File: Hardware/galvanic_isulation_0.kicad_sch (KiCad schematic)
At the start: 14 parts

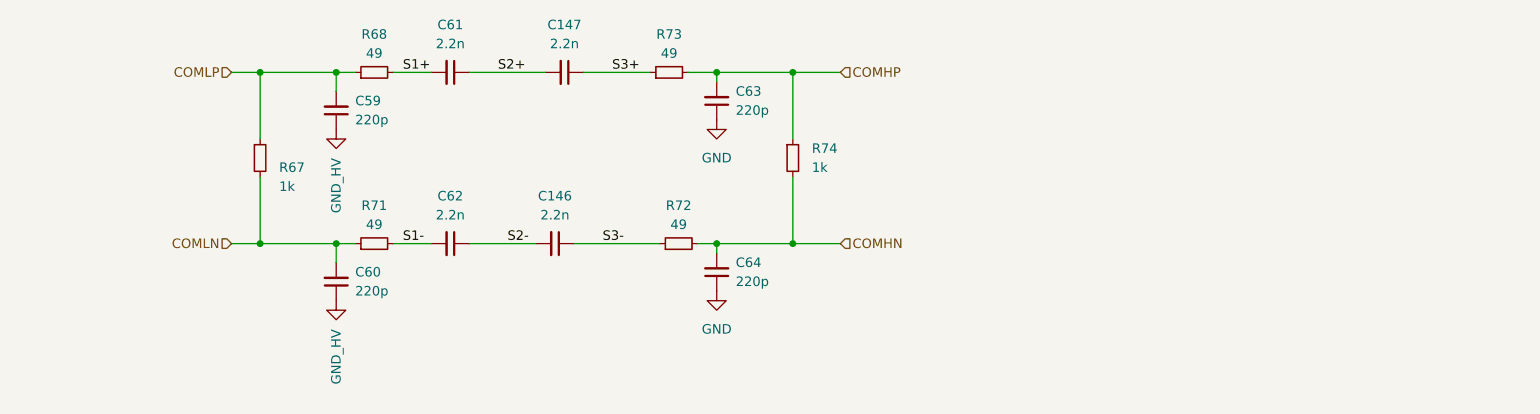
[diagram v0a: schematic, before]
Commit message: Bms plug and play, 2nd iteration with the same pinout
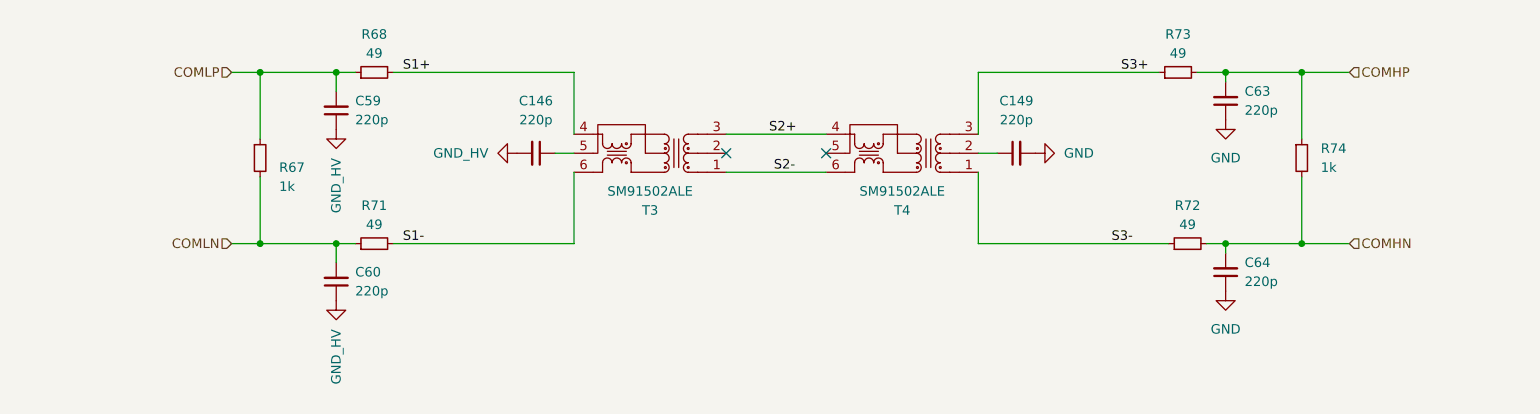
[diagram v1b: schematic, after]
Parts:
- removed C147, C61, C62: 2.2n, footrpint:CAPC5728X280N, symbol Device:C_Small
- added C149: 220p, Capacitor_SMD:C_0603_1608Metric_Pad1.08x0.95mm_HandSolder, symbol Device:C_Small
- added T3, T4: SM91502ALE, footrpint:SOP254P927X572-6N, symbol Samacsys:SM91502ALE
- C146: value 2.2n -> 220p; footprint footrpint:CAPC5728X280N -> Capacitor_SMD:C_0603_1608Metric_Pad1.08x0.95mm_HandSolder
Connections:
- net GND: now also C149.2
- net GND_HV: now also C146.2
- net S1+: now also T3.4 (SEC_1)
- net S1-: now also T3.6 (SEC_3)
- net S2+: now also T3.3 (PRI_3), T4.4 (SEC_1)
- net S2-: now also T3.1 (PRI_1), T4.6 (SEC_3); no longer C146.2
- net S3+: now also T4.3 (PRI_3)
- net S3-: now also T4.1 (PRI_1); no longer C146.1
- new net: C149.1, T4.2 (PRI_2)
- new net: C146.1, T3.5 (SEC_2)
- no-connect marks 0 -> 2
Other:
- moved on the sheet: C63, C64, R72, R73, R74

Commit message: New connectors jst_xh for low voltage side of bms
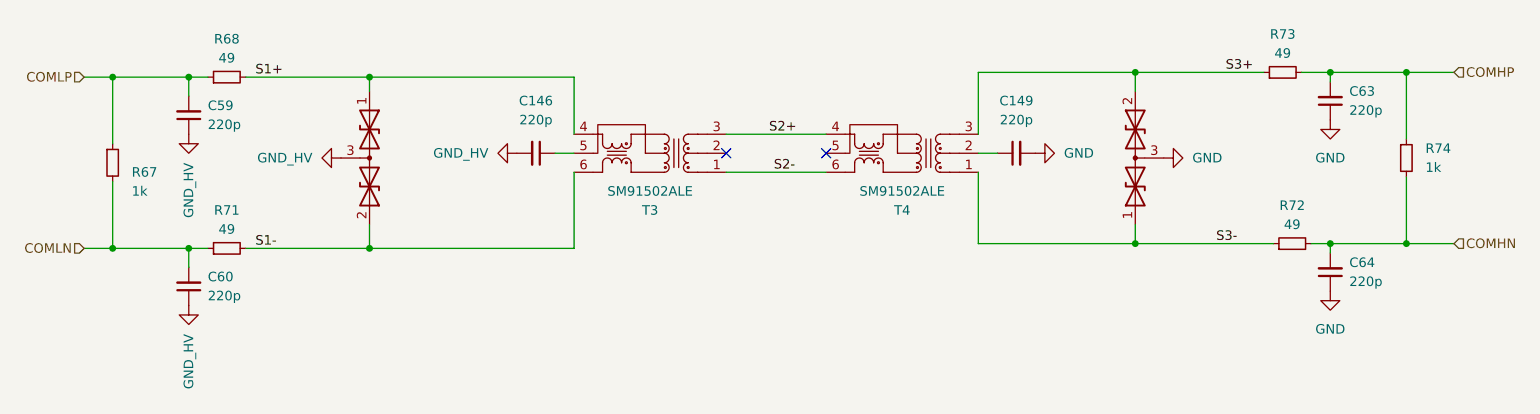
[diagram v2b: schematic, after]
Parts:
- added D42, D43: 13.3V tvs, Package_TO_SOT_SMD:SOT-23, symbol Device:D_TVS_Dual_AAC
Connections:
- net GND: now also D43.3 (common)
- net GND_HV: now also D42.3 (common)
- net S1+: now also D42.1 (A1)
- net S1-: now also D42.2 (A2)
- net S3+: now also D43.2 (A2)
- net S3-: now also D43.1 (A1)
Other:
- title: (none) -> Battery Management System for a high power gokart battery
- moved on the sheet: C59, C60, C63, C64, R67, R68, R71, R72, R73, R74
